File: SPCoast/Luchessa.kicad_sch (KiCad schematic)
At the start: 52 parts, among them SW7783 783, SW7795 795, SW7799 799

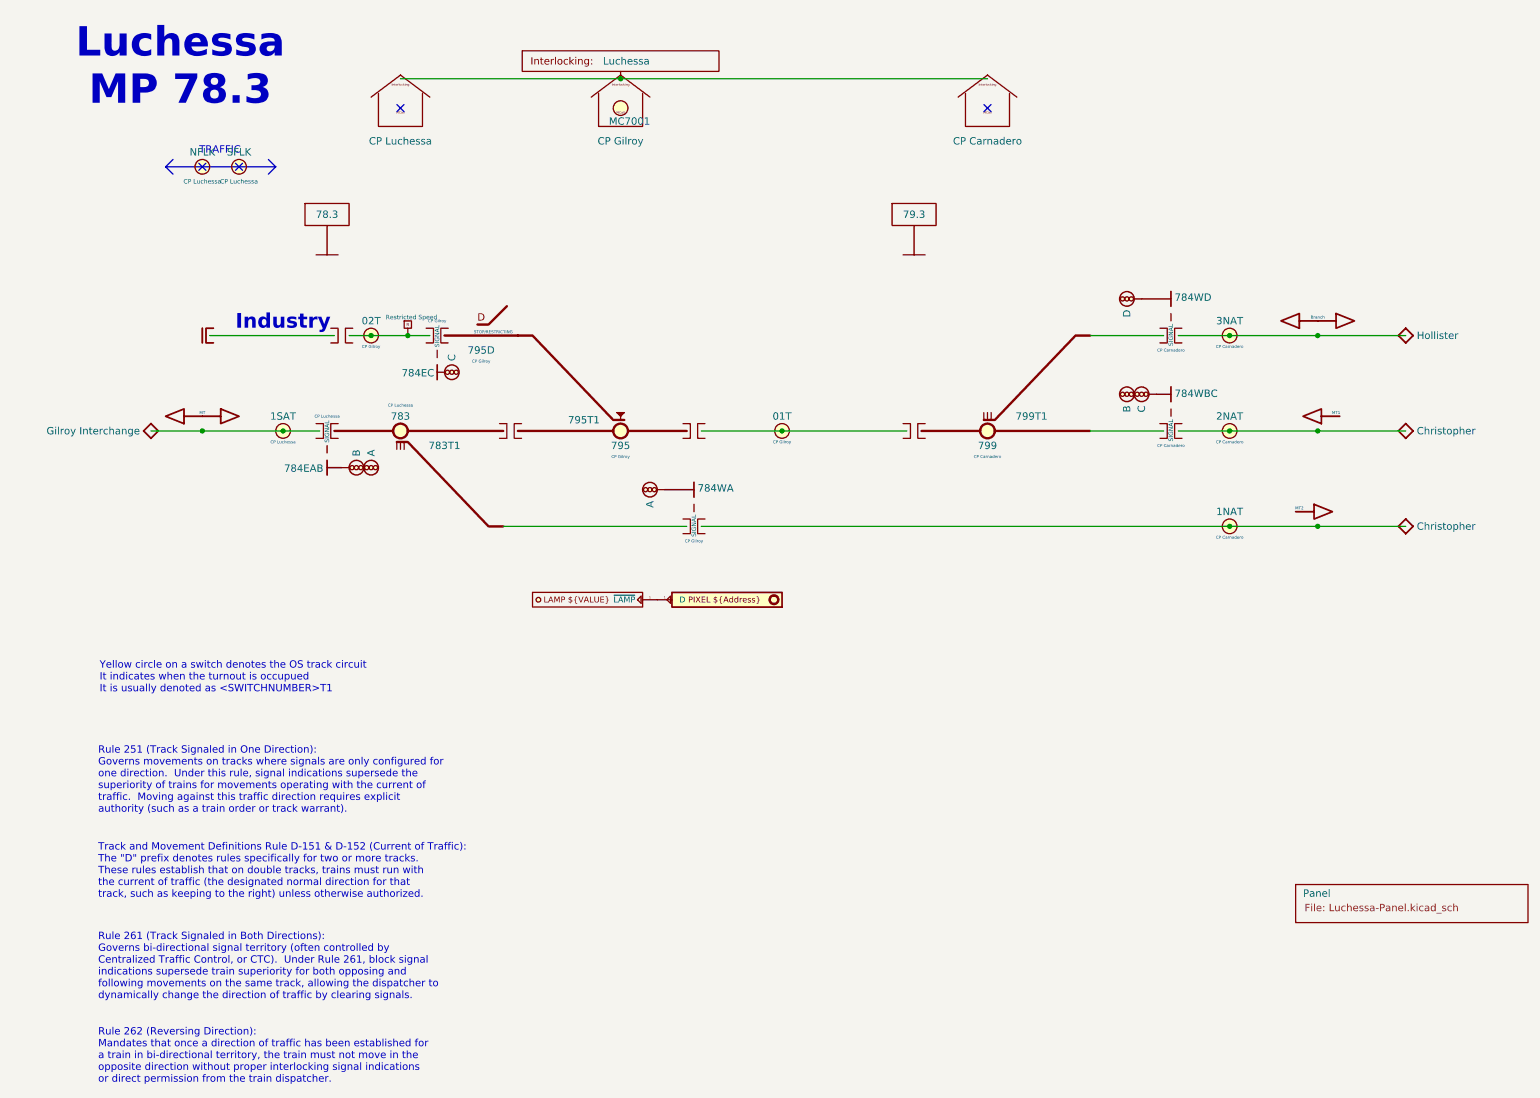
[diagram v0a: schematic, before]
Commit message: chore(kicad): owner mockup: explicit seam wiring on Luchessa and South-cTc, host and bus pins
Owner's edits, committed as they stand (2026-10-21), before scripted edits build on them.

- Interlocking gains Codeline and Host pins; MAIN HOUSE's Interlocking pin is Codeline.
- OfficeUnit gains Host and Codeline pins; JohnCTC desk processor drawn on South-cTc.
- Processor gains Transport and IO pins; MAX7313 and MCP23017 gain an I2C bus pin.
- Transports: Codeline pin renamed Host; JMRI_MQTT instance added; Loconet removed.
- Encodings' pin renamed Transport; Luchessa's 506 and Bit Packing instances removed.
- SPCoastApp virtual host (FieldUnit_Virtual) hosts CMRInet and JMRI_MQTT.
- Luchessa: unit, houses and Time Coded on one net; Host to its own processor;
  panel MAX7313s on the desk bus (OfficeBus).
- Watsonville, Caltrain, Interchange: first-pass Processor placeholders, to be redrawn.

Verified: netlist and ERC exported from the saved project; field diff against the
committed netlist shows no per-instance field lost.
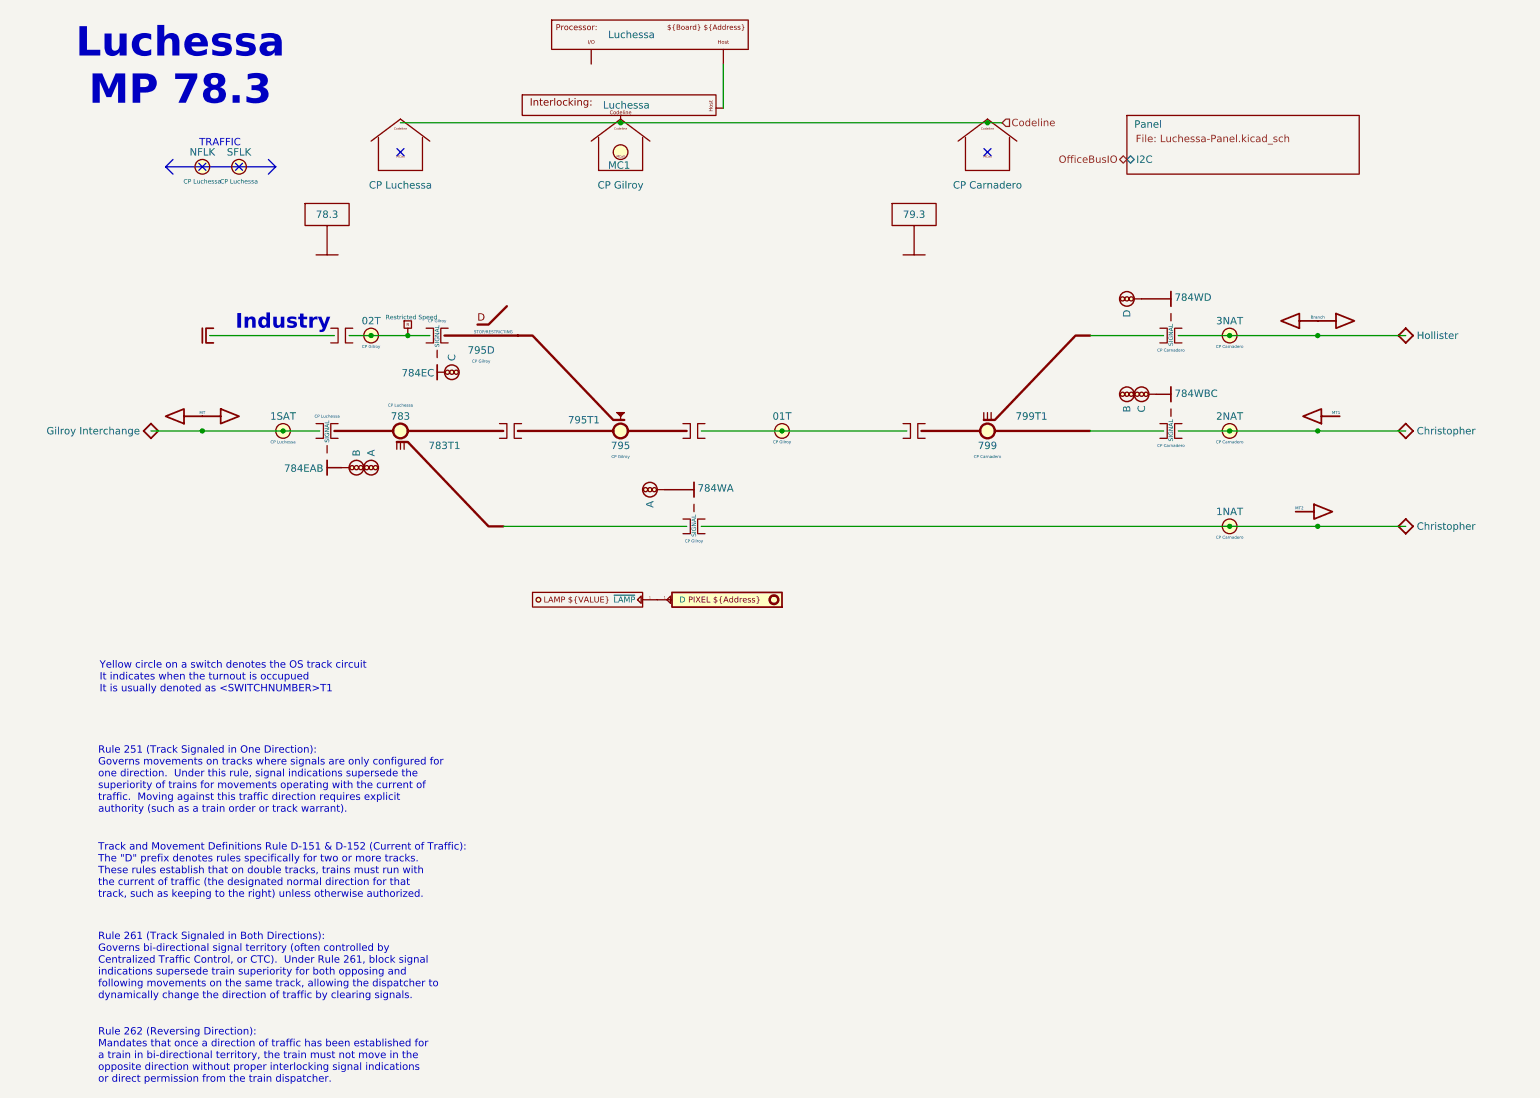
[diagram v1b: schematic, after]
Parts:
- added Proc5: Luchessa, symbol Railroad-HardwareIO:Processor
- MC7001: value (none) -> MC1
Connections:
- net Codeline: now reaches HOUSE7001.2 (Codeline), HOUSE7002.2 (Codeline), HOUSE7003.2 (Codeline), Plant7001.1 (Codeline)
- new net: Plant7001.2 (Host), Proc5.1 (Transport)
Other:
- sheet Panel ports: added I2C; removed none
